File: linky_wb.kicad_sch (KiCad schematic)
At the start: 26 parts, among them J1 Conn_01x03_Pin, Q1 BS170F, SW1 SW1, U1 TPS78230DDC, U2 MCP9700AT-ETT

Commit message: schematics: cleanup bom
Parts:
- R1, R13: value 5.1k -> 10k
- R10: value 330 -> 0
- R12: value 5.1k -> 1.2k
- R7: value 220k -> 10k
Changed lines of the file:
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@@
 			)
 		)
-		(property "Value" "330"
+		(property "Value" "0"
 			(at 57.15 128.27 90)
 			(effects
@@
 		(dnp no)
 		(property "Reference" "R12"
-			(at 161.29 40.64 0)
-			(effects
-				(font
-					(size 1.27 1.27)
-				)
-				(justify left)
-			)
-		)
-		(property "Value" "5.1k"
-			(at 165.1 41.91 90)
+			(at 160.02 40.894 0)
+			(effects
+				(font
+					(size 1.27 1.27)
+				)
+				(justify left)
+			)
+		)
+		(property "Value" "1.2k"
+			(at 165.1 42.926 90)
 			(effects
 				(font
@@
 			)
 		)
-		(property "Value" "220k"
-			(at 50.8 137.16 90)
+		(property "Value" "10k"
+			(at 50.8 136.398 90)
 			(effects
 				(font
@@
 		(dnp no)
 		(property "Reference" "R13"
-			(at 199.39 20.32 0)
-			(effects
-				(font
-					(size 1.27 1.27)
-				)
-				(justify left)
-			)
-		)
-		(property "Value" "5.1k"
-			(at 203.2 21.59 90)
+			(at 197.866 20.574 0)
+			(effects
+				(font
+					(size 1.27 1.27)
+				)
+				(justify left)
+			)
+		)
+		(property "Value" "10k"
+			(at 203.2 21.844 90)
 			(effects
 				(font
@@
 			)
 		)
-		(property "Value" "5.1k"
-			(at 173.99 38.1 90)
-			(effects
-				(font
+		(property "Value" "10k"
+			(at 173.99 38.862 90)
+			(effects
+				(font

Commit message: 1.0.0 boards sent to production
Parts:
- C1, C2: LCSC (none) -> C19666
- C19, C3: LCSC (none) -> C1525
- D1, D2: LCSC (none) -> C19726
- D6: LCSC (none) -> C108793
- J1, TP1, TP2, TP4, TP6: now left out of the parts list
- OC1: LCSC (none) -> C125118
- Q1: LCSC (none) -> C151050
- R1, R13: LCSC (none) -> C25744
- R10: LCSC (none) -> C25104
- R12: value 1.2k -> 1.5k; LCSC (none) -> C25867
- R5, R6, R9: value 5.1k -> 1.5k; LCSC (none) -> C25867
- R7: LCSC (none) -> C25767
- SW1: LCSC (none) -> C221880
- U1: LCSC (none) -> C90840
- U2: LCSC (none) -> C127949
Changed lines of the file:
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@@
+			)
+		)
+		(property "LCSC" "C19666"
+			(at 213.741 66.1416 0)
+			(effects
+				(font
+					(size 1.27 1.27)
+				)
+				(hide yes)
 			)
 		)
@@
 			)
 		)
+		(property "LCSC" "C25104"
+			(at 57.15 125.73 0)
+			(effects
+				(font
+					(size 1.27 1.27)
+				)
+				(hide yes)
+			)
+		)
 		(pin "1"
 		)
@@
 		(at 246.38 60.96 270)
 		(unit 1)
-		(exclude_from_sim no)
-		(in_bom yes)
+		(exclude_from_sim yes)
+		(in_bom no)
 		(on_board yes)
 		(dnp no)
@@
 			)
 		)
+		(property "LCSC" "C1525"
+			(at 203.2 64.77 0)
+			(effects
+				(font
+					(size 1.27 1.27)
+				)
+				(hide yes)
+			)
+		)
 		(pin "1"
 		)
@@
 			)
 		)
-		(property "Value" "5.1k"
+		(property "Value" "1.5k"
 			(at 106.68 135.89 90)
 			(effects
@@
 			)
 		)
+		(property "LCSC" "C25867"
+			(at 107.95 137.16 0)
+			(effects
+				(font
+					(size 1.27 1.27)
+				)
+				(hide yes)
+			)
+		)
 		(pin "1"
 		)
@@
 			)
 		)
-		(property "Value" "1.2k"
+		(property "Value" "1.5k"
 			(at 165.1 42.926 90)
 			(effects
@@
 		(property "price x100" "0.0002"
 			(at 165.1 40.64 0)
+			(effects
+				(font
+					(size 1.27 1.27)
+				)
+				(hide yes)
+			)
+		)
+		(property "LCSC" "C25867"
+			(at 160.02 40.894 0)
 			(effects
 				(font
@@
 			)
 		)
-		(property "Value" "5.1k"
+		(property "Value" "1.5k"
 			(at 101.6 135.89 90)
 			(effects
@@
 			)
 		)
+		(property "LCSC" "C25867"
+			(at 97.79 137.16 0)
+			(effects
+				(font
+					(size 1.27 1.27)
+				)
+				(hide yes)
+			)
+		)
 		(pin "1"
 		)
@@
 			)
 		)
+		(property "LCSC" "C127949"
+			(at 132.08 104.1399 0)
+			(effects
+				(font
+					(size 1.27 1.27)
+				)
+				(hide yes)
+			)
+		)
 		(pin "1"
 		)
@@
 		(unit 1)
 		(exclude_from_sim no)
-		(in_bom yes)
+		(in_bom no)
 		(on_board yes)
 		(dnp no)
@@
 		(unit 1)
 		(exclude_from_sim no)
-		(in_bom yes)
+		(in_bom no)
 		(on_board yes)
 		(dnp no)
@@
 			)
 		)
+		(property "LCSC" "C25767"
+			(at 49.3014 133.4516 0)
+			(effects
+				(font
+					(size 1.27 1.27)
+				)
+				(hide yes)
+			)
+		)
 		(pin "1"
 		)
@@
 			)
 		)
+		(property "LCSC" "C19726"
+			(at 187.96 60.9599 0)
+			(effects
+				(font
+					(size 1.27 1.27)
+				)
+				(hide yes)
+			)
+		)
 		(pin "1"
 		)
@@
 		(unit 1)
 		(exclude_from_sim no)
-		(in_bom yes)
+		(in_bom no)
 		(on_board yes)
 		(dnp no)
@@
 			)
 		)
+		(property "LCSC" "C221880"
+			(at 44.45 121.031 0)
+			(effects
+				(font
+					(size 1.27 1.27)
+				)
+				(hide yes)
+			)
+		)
 		(pin "1"
 		)
@@
 			)
 		)
+		(property "LCSC" "C19666"
+			(at 246.761 66.1416 0)
+			(effects
+				(font
+					(size 1.27 1.27)
+				)
+				(hide yes)
+			)
+		)
 		(pin "1"
 		)
@@
 		(property "price x100" "0.0002"
 			(at 203.2 20.32 0)
+			(effects
+				(font
+					(size 1.27 1.27)
+				)
+				(hide yes)
+			)
+		)
+		(property "LCSC" "C25744"
+			(at 197.866 20.574 0)
 			(effects
 				(font
@@
 			)
 		)
+		(property "LCSC" "C151050"
+			(at 207.01 30.4799 0)
+			(effects
+				(font
+					(size 1.27 1.27)
+				)
+				(hide yes)
+			)
+		)
 		(pin "1"
 		)
@@
 			)
 		)
-		(property "Value" "5.1k"
+		(property "Value" "1.5k"
 			(at 96.52 135.89 90)
 			(effects
@@
 		(property "price x100" "0.0002"
 			(at 96.52 137.16 0)
+			(effects
+				(font
+					(size 1.27 1.27)
+				)
+				(hide yes)
+			)
+		)
+		(property "LCSC" "C25867"
+			(at 97.79 137.16 0)
 			(effects
 				(font
@@
 			)
 		)
+		(property "LCSC" "C108793"
+			(at 93.218 127.1016 0)
+			(effects
+				(font
+					(size 1.27 1.27)
+				)
+				(hide yes)
+			)
+		)
 		(pin "1"
 		)
@@
 		(property "price x100" "0.43"
 			(at 231.14 63.5 0)
+			(effects
+				(font
+					(size 1.27 1.27)
+				)
+				(hide yes)
+			)
+		)
+		(property "LCSC" "C90840"
+			(at 231.14 54.1782 0)
 			(effects
 				(font
@@
 			)
 		)
+		(property "LCSC" "C125118"
+			(at 177.8 24.1299 0)
+			(effects
+				(font
+					(size 1.27 1.27)
+				)
+				(hide yes)
+			)
+		)
 		(pin "4"
 		)
@@
 			)
 		)
+		(property "LCSC" "C19726"
+			(at 177.8 60.9599 0)
+			(effects
+				(font
+					(size 1.27 1.27)
+				)
+				(hide yes)
+			)
+		)
 		(pin "1"
 		)
@@
 			)
 		)
+		(property "LCSC" "C25744"
+			(at 170.18 36.83 0)
+			(effects
+				(font
+					(size 1.27 1.27)
+				)
+				(hide yes)
+			)
+		)
 		(pin "1"
 		)
@@
 		(property "Description" ""
 			(at 121.92 105.41 0)
+			(effects
+				(font
+					(size 1.27 1.27)
+				)
+				(hide yes)
+			)
+		)
+		(property "LCSC" "C1525"
+			(at 123.19 102.87 0)
 			(effects
 				(font
@@
 		(unit 1)
 		(exclude_from_sim no)
-		(in_bom yes)
-		(on_board yes)
-		(dnp no)
+		(in_bom no)
+		(on_board yes)
+		(dnp no)

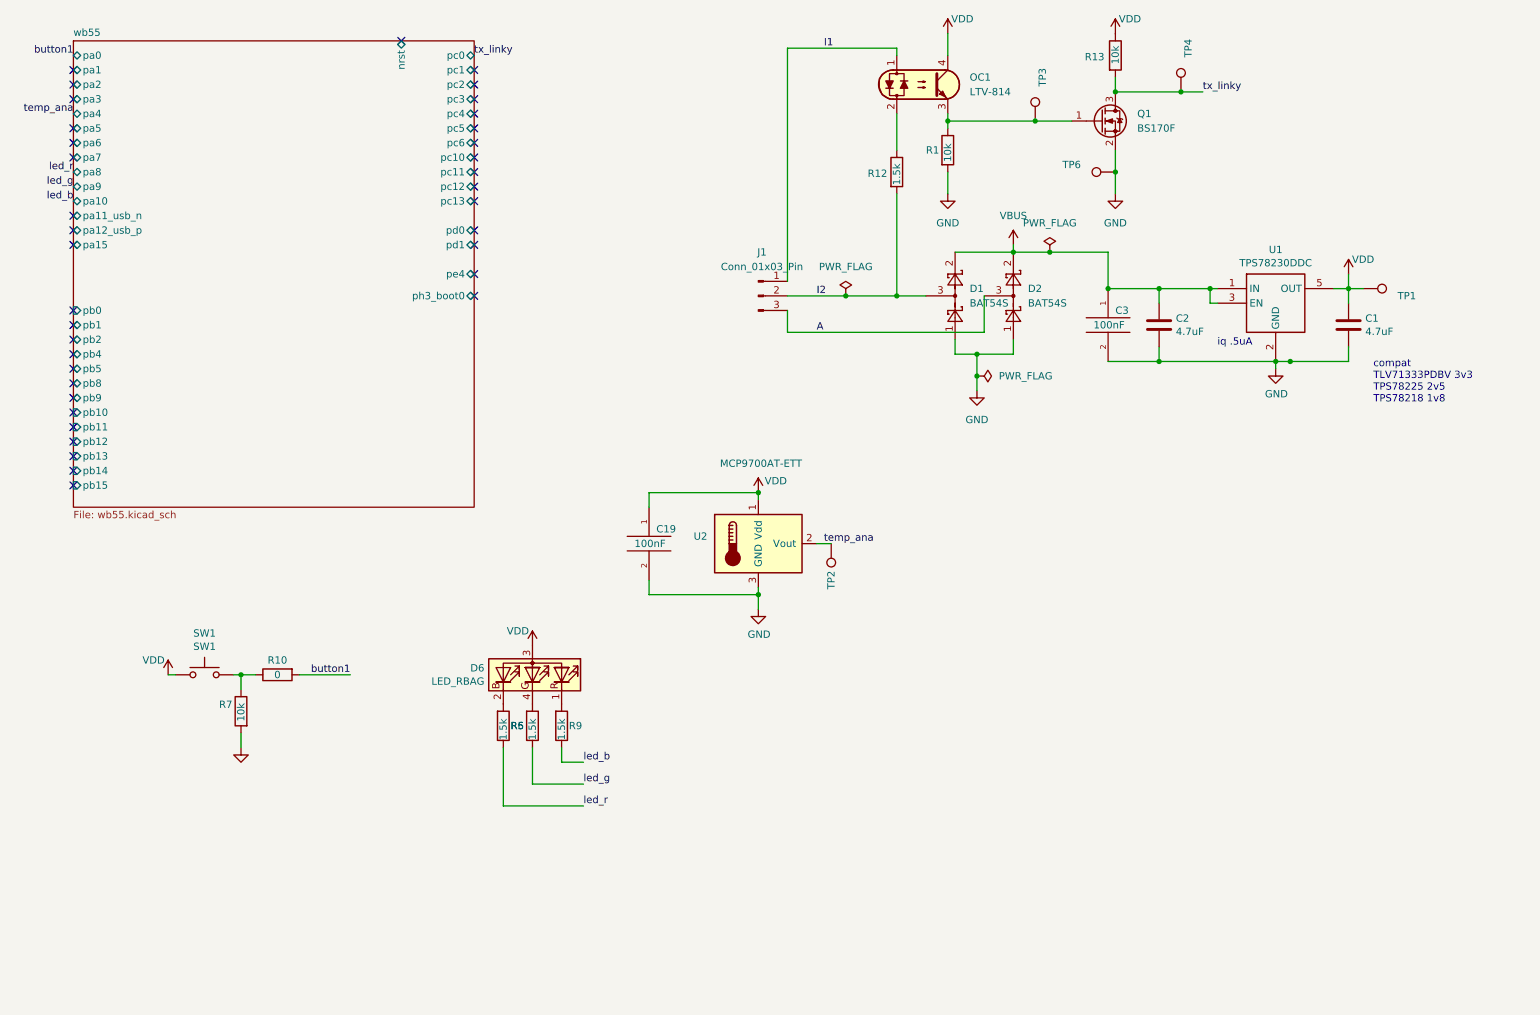
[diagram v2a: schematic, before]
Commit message: cleanups, exclude some drcs, fix antenna symbol to avoid ground disconnection, tweak ci
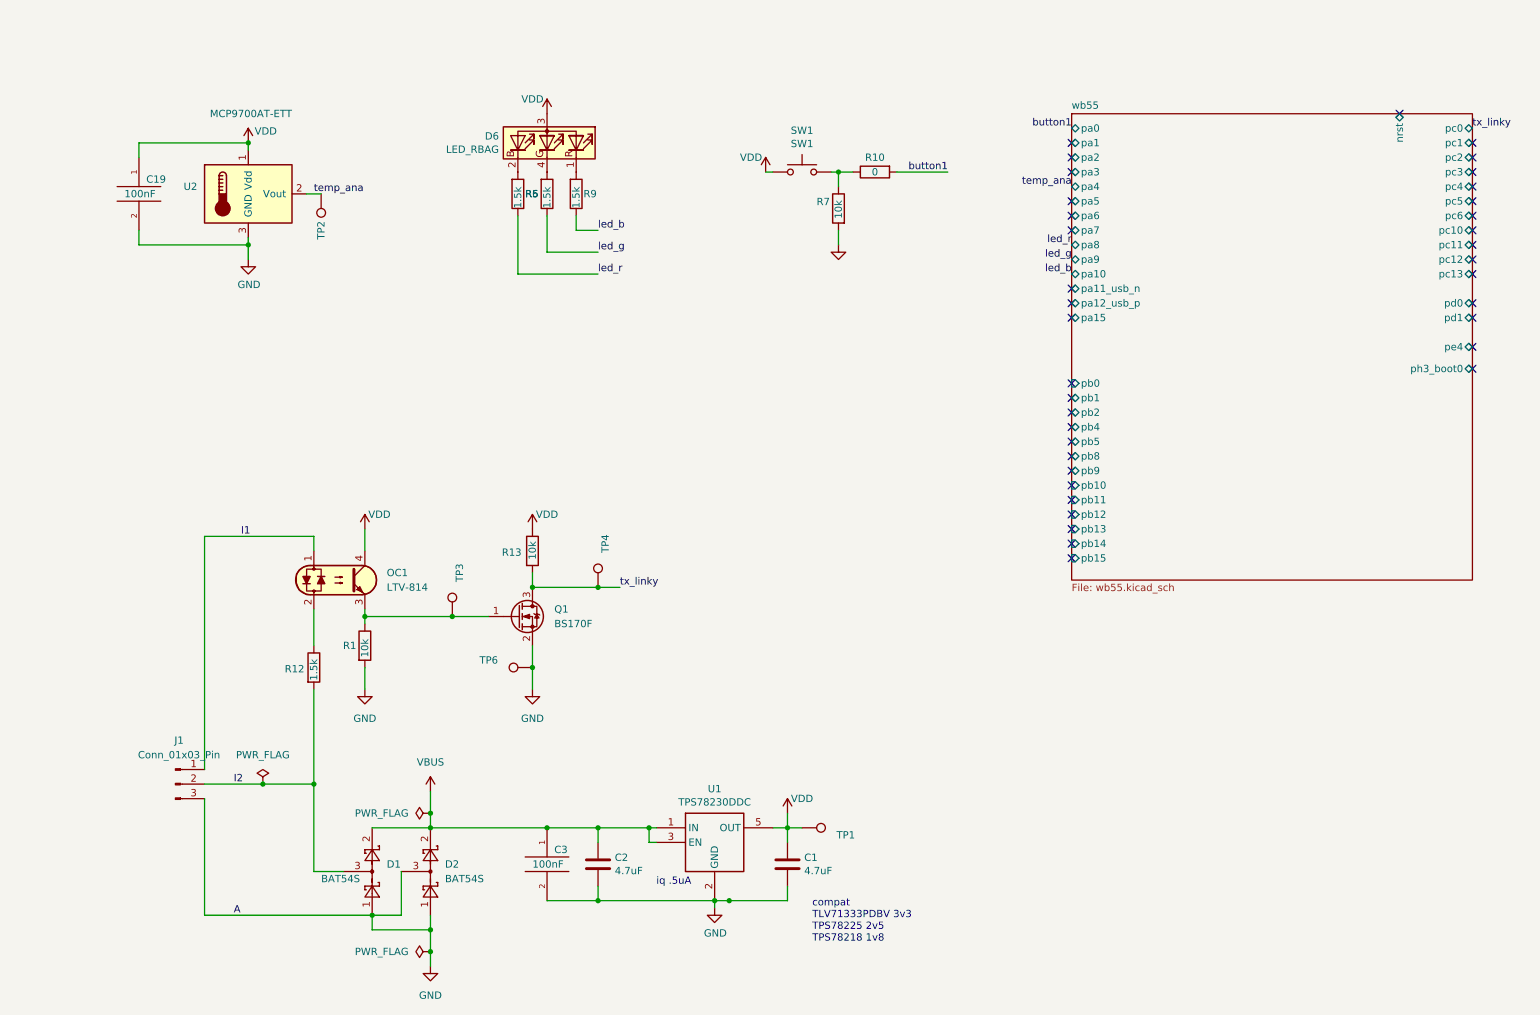
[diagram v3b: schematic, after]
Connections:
- net A is gone; now on net GND: D2.3, J1.3 (Pin_3)
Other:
- moved on the sheet: C1, C19, C2, C3, D1, D2, D6, J1, OC1, Q1, R1, R10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
